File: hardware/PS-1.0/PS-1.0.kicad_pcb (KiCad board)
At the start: 2 copper layers, 98.4 x 199.4 mm, 46 parts, among them J1 Conn_02x16_Odd_Even, J2 Conn_01x05, J3 Conn_01x05, J8 Conn_01x03, J9 Conn_01x03, K1 RAYEX-L90, K2 RAYEX-L90, Q1 IRFPE50, Q2 IRFPE50, Q3 IRFPE50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

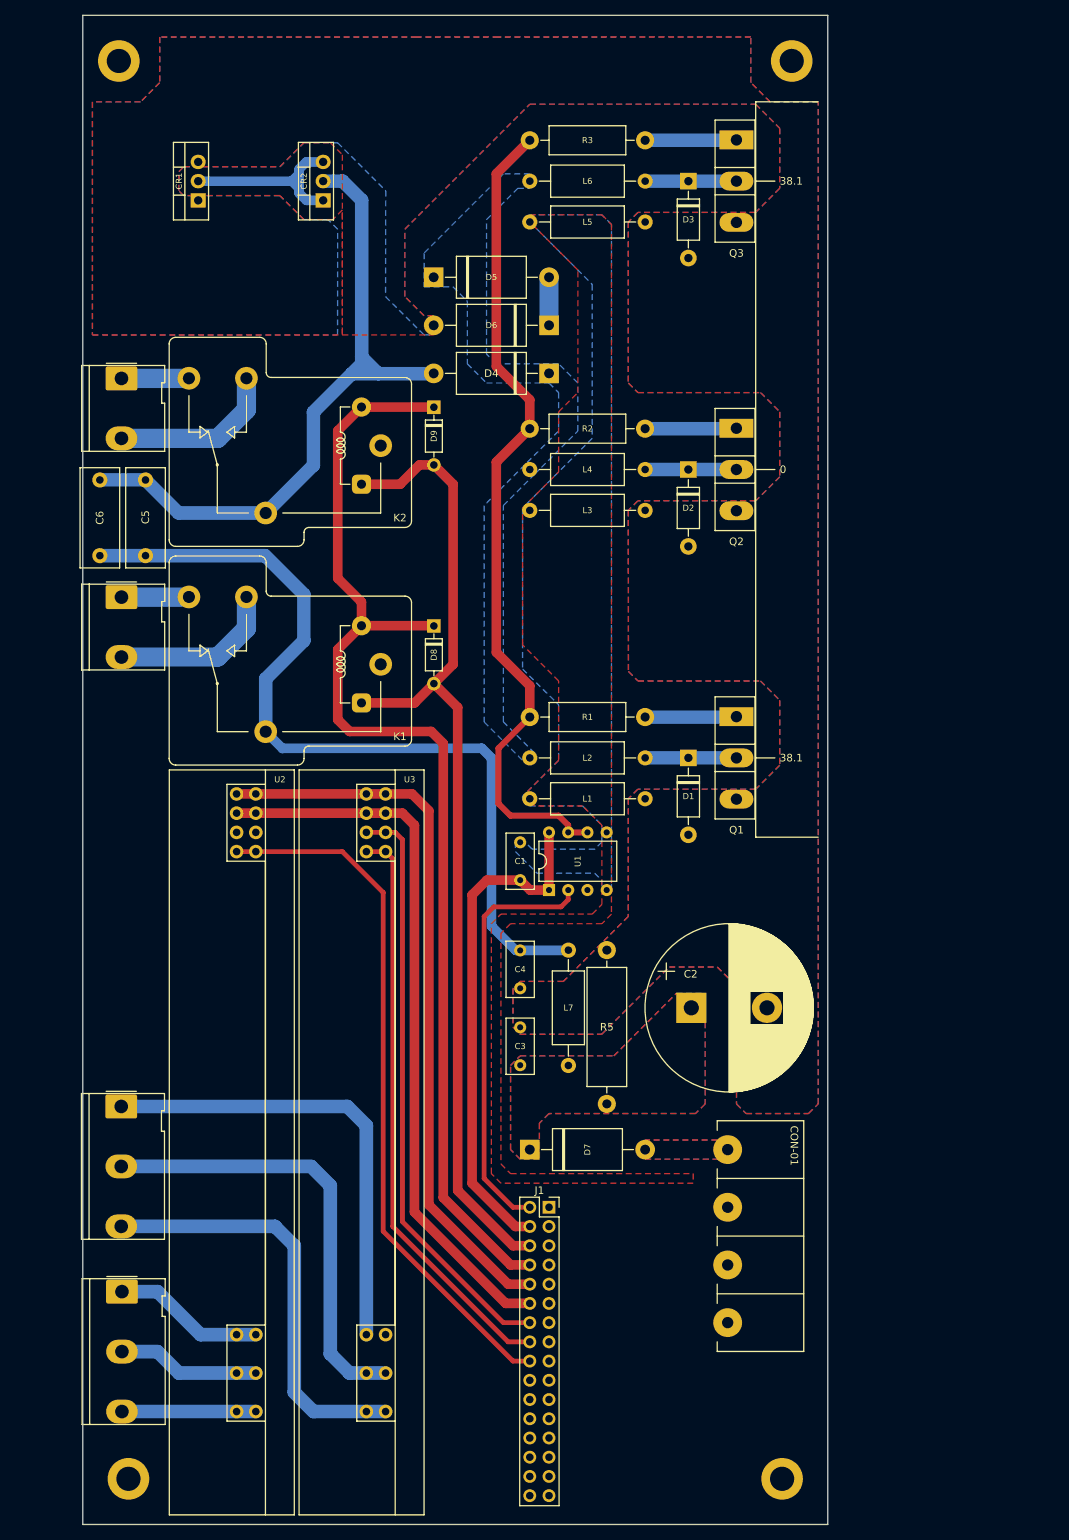
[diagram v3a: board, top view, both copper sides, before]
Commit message: new file:   hardware/Gain/Gain-backups/Gain-2025-04-17_151501.zip 	deleted:    hardware/MSD-1.0/MSD-1.0-backups/MSD-1.0-2025-03-25_151318.zip 	deleted:    hardware/MSD-1.0/MSD-1.0-backups/MSD-1.0-2025-03-26_084506.zip 	deleted:    hardware/MSD-1.0/MSD-1.0-backups/MSD-1.0-2025-03-26_085636.zip 	deleted:    hardware/MSD-1.0/MSD-1.0-backups/MSD-1.0-2025-03-26_090649.zip 	new file:   hardware/MSD-1.0/MSD-1.0-backups/MSD-1.0-2025-04-17_090027.zip 	new file:   hardware/MSD-1.0/MSD-1.0-backups/MSD-1.0-2025-04-17_092653.zip 	new file:   hardware/MSD-1.0/MSD-1.0-backups/MSD-1.0-2025-04-17_105503.zip 	new file:   hardware/MSD-1.0/MSD-1.0-backups/MSD-1.0-2025-04-17_154051.zip 	modified:   hardware/MSD-1.0/MSD-1.0.kicad_pcb 	modified:   hardware/MSD-1.0/MSD-1.0.step 	deleted:    hardware/PS-1.0/PS-1.0-backups/PS-1.0-2025-03-19_103853.zip 	deleted:    hardware/PS-1.0/PS-1.0-backups/PS-1.0-2025-03-19_155128.zip 	deleted:    hardware/PS-1.0/PS-1.0-backups/PS-1.0-2025-03-24_095559.zip 	deleted:    hardware/PS-1.0/PS-1.0-backups/PS-1.0-2025-03-24_110339.zip 	deleted:    hardware/PS-1.0/PS-1.0-backups/PS-1.0-2025-03-24_111100.zip 	deleted:    hardware/PS-1.0/PS-1.0-backups/PS-1.0-2025-04-16_154157.zip 	deleted:    hardware/PS-1.0/PS-1.0-backups/PS-1.0-2025-04-16_154838.zip 	new file:   hardware/PS-1.0/PS-1.0-backups/PS-1.0-2025-04-16_163259.zip 	new file:   hardware/PS-1.0/PS-1.0-backups/PS-1.0-2025-04-17_105409.zip 	new file:   hardware/PS-1.0/PS-1.0-backups/PS-1.0-2025-04-17_110908.zip 	new file:   hardware/PS-1.0/PS-1.0-backups/PS-1.0-2025-04-17_114838.zip 	new file:   hardware/PS-1.0/PS-1.0-backups/PS-1.0-2025-04-17_155117.zip 	new file:   hardware/PS-1.0/PS-1.0-backups/PS-1.0-2025-04-17_155935.zip 	new file:   hardware/PS-1.0/PS-1.0-backups/PS-1.0-2025-04-17_160519.zip 	modified:   hardware/PS-1.0/PS-1.0.kicad_pcb 	modified:   hardware/PS-1.0/PS-1.0.kicad_prl 	modified:   hardware/PS-1.0/PS-1.0.kicad_pro 	modified:   hardware/PS-1.0/PS-1.0.kicad_sch 	modified:   hardware/PS-1.0/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
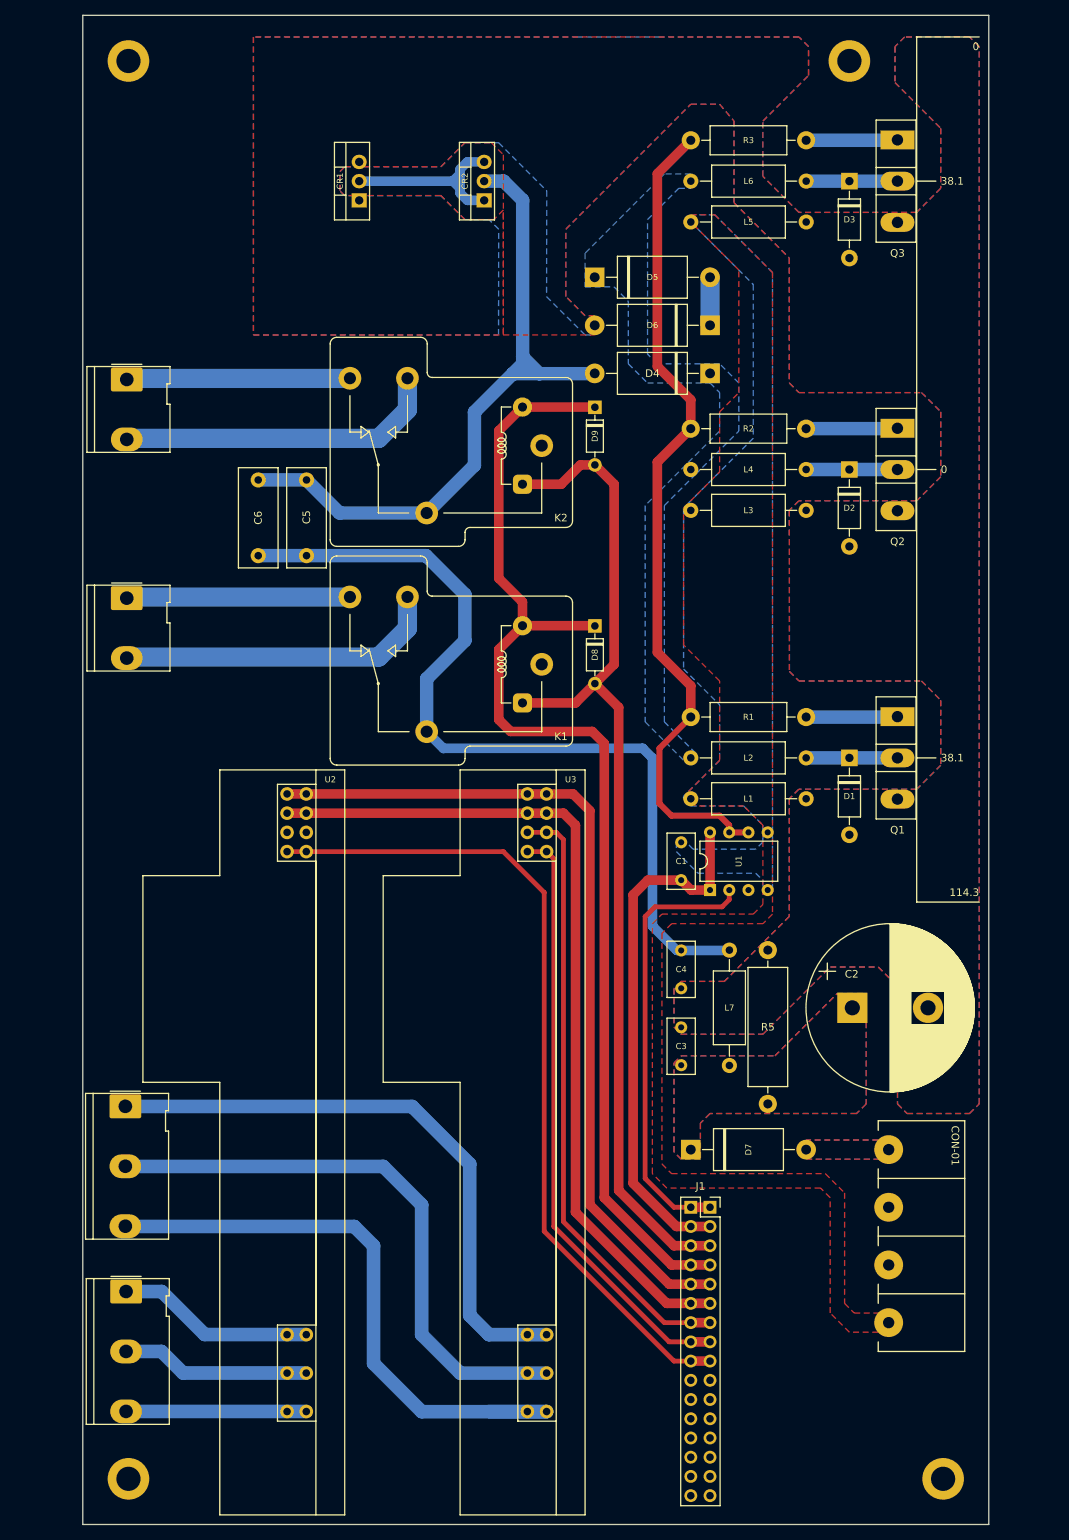
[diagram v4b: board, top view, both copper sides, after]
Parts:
- J1: value Conn_02x16_Odd_Even -> Conn_01x16; footprint Connector_PinSocket_2.54mm:PinSocket_2x16_P2.54mm_Vertical -> Connector_PinSocket_2.54mm:PinSocket_1x16_P2.54mm_Vertical_2
- U2: footprint Custom:ESU-REM-3.0 -> Custom:ESU-REM-4.0
- U3: footprint Custom:ESU-REM-3.0 -> Custom:ESU-MSD-1.0
- moved Q2 21.3 mm to (228.3, 83.8)
- moved C1 21.3 mm to (199.7, 143.5)
- moved C3 21.3 mm to (199.7, 167.9)
- moved C4 21.3 mm to (199.7, 152.8)
- moved C5 21.3 mm to (150.2, 90.6)
- moved CR2 21.3 mm to (173.7, 53.7)
- moved D1 21.3 mm to (221.9, 127.3)
- moved D2 21.3 mm to (221.9, 89.2)
- moved D3 21.3 mm to (221.9, 51.1)
- moved D4 21.3 mm to (203.5, 76.5)
- moved D5 21.3 mm to (188.3, 63.8)
- moved D6 21.3 mm to (203.5, 70.2)
- moved D8 21.3 mm to (188.3, 109.9)
- moved D9 21.3 mm to (188.3, 81.0)
- moved H2 21.3 mm to (234.3, 222.6)
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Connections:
- J1 pad 1: unconnected-(J1-Pin_1-Pad1) -> /PWM
- J1 pad 10: Net-(J1-Pin_10) -> unconnected-(J1-Pin_10-Pad10)
- J1 pad 12: Net-(J1-Pin_12) -> unconnected-(J1-Pin_12-Pad12)
- J1 pad 14: Net-(J1-Pin_14) -> unconnected-(J1-Pin_14-Pad14)
- J1 pad 16: Net-(J1-Pin_16) -> unconnected-(J1-Pin_16-Pad16)
- J1 pad 2: /PWM -> VDD
- J1 pad 3: unconnected-(J1-Pin_3-Pad3) -> /RLY-A
- J1 pad 4: VDD -> /RLY-K
- J1 pad 5: unconnected-(J1-Pin_5-Pad5) -> Net-(J1-Pin_5)
- J1 pad 6: /RLY-A -> Net-(J1-Pin_6)
- J1 pad 7: unconnected-(J1-Pin_7-Pad7) -> Net-(J1-Pin_7)
- J1 pad 8: /RLY-K -> Net-(J1-Pin_8)
- J1 pad 9: unconnected-(J1-Pin_9-Pad9) -> Net-(J1-Pin_9)
- U2 pad 1: Net-(J1-Pin_10) -> Net-(J1-Pin_5)
- U2 pad 2: Net-(J1-Pin_12) -> Net-(J1-Pin_6)
- U2 pad 4: Net-(J1-Pin_18) -> Net-(J1-Pin_9)
- U3 pad 1: Net-(J1-Pin_10) -> Net-(J1-Pin_5)
- U3 pad 2: Net-(J1-Pin_12) -> Net-(J1-Pin_6)
- U3 pad 3: Net-(J1-Pin_14) -> Net-(J1-Pin_7)
- U3 pad 4: Net-(J1-Pin_16) -> Net-(J1-Pin_8)
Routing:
- net Net-(J1-Pin_5): track 0.00 -> 113.2 mm
- net Net-(J1-Pin_6): track 0.00 -> 112.7 mm
- net Net-(J1-Pin_9): track 0.00 -> 110.0 mm
- net Net-(J1-Pin_10): track 96.1 -> 0.00 mm
- net Net-(J1-Pin_12): track 95.5 -> 0.00 mm
- net Net-(J1-Pin_18): track 92.8 -> 0.00 mm
- net Net-(J1-Pin_7): track 0.00 -> 80.5 mm
- net Net-(J1-Pin_8): track 0.00 -> 79.4 mm
- net Net-(J1-Pin_14): track 78.0 -> 0.00 mm
- net Net-(J1-Pin_16): track 76.9 -> 0.00 mm
- net Net-(J3-Pin_5): track 56.4 -> 82.5 mm
- net Net-(J9-Pin_1): track 8.92 -> 29.6 mm
- net Net-(J8-Pin_1): track 8.92 -> 29.6 mm
- net Net-(J9-Pin_3): track 22.2 -> 42.9 mm
- net Net-(J8-Pin_3): track 22.2 -> 42.9 mm
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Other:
- board size 98.4 x 199.4 mm -> 119.7 x 199.4 mm
- board text added: "114.3"

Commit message: new file:   .~BoM.xlsx 	new file:   BoM.xlsx 	new file:   hardware/BoM.xlsx 	deleted:    hardware/MSD-1.0/MSD-1.0-backups/MSD-1.0-2025-03-26_092035.zip 	deleted:    hardware/MSD-1.0/MSD-1.0-backups/MSD-1.0-2025-03-26_092834.zip 	deleted:    hardware/MSD-1.0/MSD-1.0-backups/MSD-1.0-2025-03-27_092014.zip 	new file:   hardware/MSD-1.0/MSD-1.0-backups/MSD-1.0-2025-04-28_130614.zip 	new file:   hardware/MSD-1.0/MSD-1.0-backups/MSD-1.0-2025-04-28_131128.zip 	new file:   hardware/MSD-1.0/MSD-1.0-backups/MSD-1.0-2025-04-28_132753.zip 	new file:   hardware/MSD-1.0/MSD-1.0.csv 	modified:   hardware/MSD-1.0/MSD-1.0.kicad_pcb 	modified:   hardware/MSD-1.0/MSD-1.0.kicad_sch 	deleted:    hardware/PS-1.0/PS-1.0-backups/PS-1.0-2025-03-24_111800.zip 	deleted:    hardware/PS-1.0/PS-1.0-backups/PS-1.0-2025-03-24_112738.zip 	deleted:    hardware/PS-1.0/PS-1.0-backups/PS-1.0-2025-03-25_152833.zip 	deleted:    hardware/PS-1.0/PS-1.0-backups/PS-1.0-2025-03-25_154601.zip 	deleted:    hardware/PS-1.0/PS-1.0-backups/PS-1.0-2025-03-25_155821.zip 	deleted:    hardware/PS-1.0/PS-1.0-backups/PS-1.0-2025-04-11_101418.zip 	deleted:    hardware/PS-1.0/PS-1.0-backups/PS-1.0-2025-04-11_110528.zip 	deleted:    hardware/PS-1.0/PS-1.0-backups/PS-1.0-2025-04-11_111527.zip 	deleted:    hardware/PS-1.0/PS-1.0-backups/PS-1.0-2025-04-11_114252.zip 	deleted:    hardware/PS-1.0/PS-1.0-backups/PS-1.0-2025-04-17_105409.zip 	new file:   hardware/PS-1.0/PS-1.0-backups/PS-1.0-2025-04-19_071925.zip 	new file:   hardware/PS-1.0/PS-1.0-backups/PS-1.0-2025-04-27_222808.zip 	new file:   hardware/PS-1.0/PS-1.0-backups/PS-1.0-2025-04-27_223939.zip 	new file:   hardware/PS-1.0/PS-1.0-backups/PS-1.0-2025-04-27_224445.zip 	new file:   hardware/PS-1.0/PS-1.0-backups/PS-1.0-2025-04-27_225206.zip 	new file:   hardware/PS-1.0/PS-1.0-backups/PS-1.0-2025-04-27_230217.zip 	new file:   hardware/PS-1.0/PS-1.0-backups/PS-1.0-2025-04-28_083014.zip 	new file:   hardware/PS-1.0/PS-1.0-backups/PS-1.0-2025-04-28_112951.zip 	new file:   har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
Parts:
- added R4: 100kΩ, Resistor_THT:R_Axial_DIN0204_L3.6mm_D1.6mm_P7.62mm_Horizontal, F.Cu at (213.7, 213.4)
- added U4: PC817, Package_DIP:DIP-4_W7.62mm_Socket, F.Cu at (208.6, 217.2)
- C2: value C_Polarized -> 1000µF 160V
- C3, C4: value 100nF -> 100nF 100V
- CON-01: value Screw_Terminal_01x04 -> KF7.62-4
- CR1, CR2: value ~ -> STTH1002CT
- D1, D2, D3: value 1N47xxA -> 1N4746A
- D4: value SB5H100 -> SB5H100/ SB5100
- D5, D6: value 1.5KExxA -> 1.5KE56A
- J1: value Conn_01x16 -> PinSocket_02x16_P2.54mm_Vertical
- R1, R2, R3: value 6.2Ω -> 6.2Ω 2W
- R5: value 120Ω -> 120Ω 2W
- U1: value TC4422 -> TC4422/ TC4420
- moved J2 7.62 mm to (126.4, 190.2)
- moved J3 7.62 mm to (126.3, 165.7)
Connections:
- J1 pad 10: unconnected-(J1-Pin_10-Pad10) -> Net-(J1-Pin_10)
- J1 pad 15: unconnected-(J1-Pin_15-Pad15) -> Net-(CON-01-Pin_2)
- J1 pad 16: unconnected-(J1-Pin_16-Pad16) -> GND
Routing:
- net Net-(R4-Pad1): track 0.00 -> 8.68 mm
- net Net-(J3-Pin_1): track 79.8 -> 87.5 mm
- net Net-(J3-Pin_5): track 82.5 -> 90.1 mm
- net Net-(J3-Pin_3): track 77.0 -> 84.6 mm
- net Net-(J1-Pin_10): track 0.00 -> 7.62 mm
- net Net-(J2-Pin_1): track 26.1 -> 29.3 mm
- net Net-(J2-Pin_5): track 23.8 -> 27.0 mm
- net Net-(J2-Pin_3): track 25.0 -> 28.2 mm
- added copper zone on B.Cu, net Net-(CON-01-Pin_2)
